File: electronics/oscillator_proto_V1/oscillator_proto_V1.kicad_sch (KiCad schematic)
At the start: 48 parts, among them J1 module_2x15_left_input, J2 module_2x15_right_input, J3 Coax, Q1 BC337, U1 TL081, U2 LME49720, U3 TL082, U4 TL431

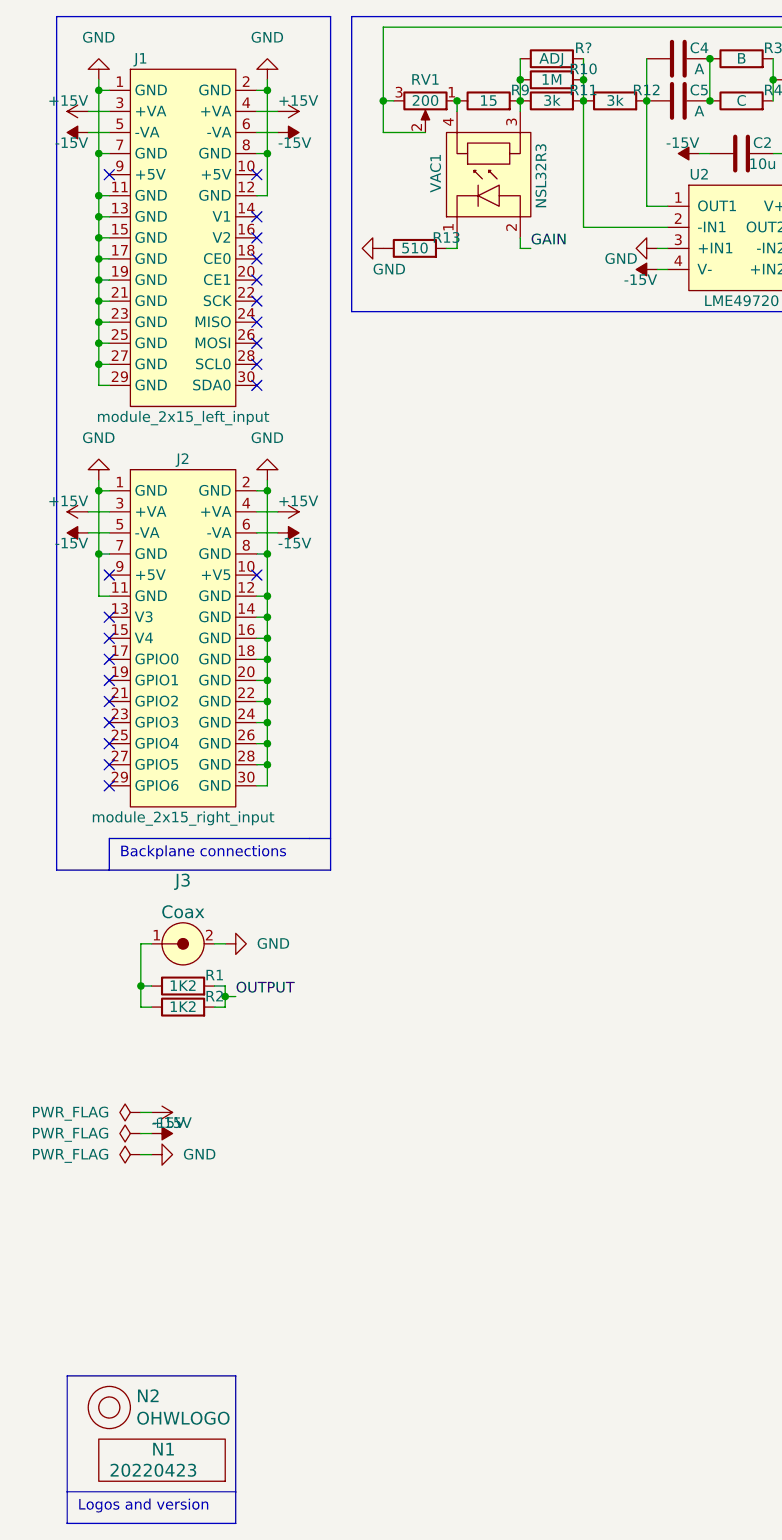
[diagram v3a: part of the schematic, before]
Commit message: added additional adjust resistor and updated values
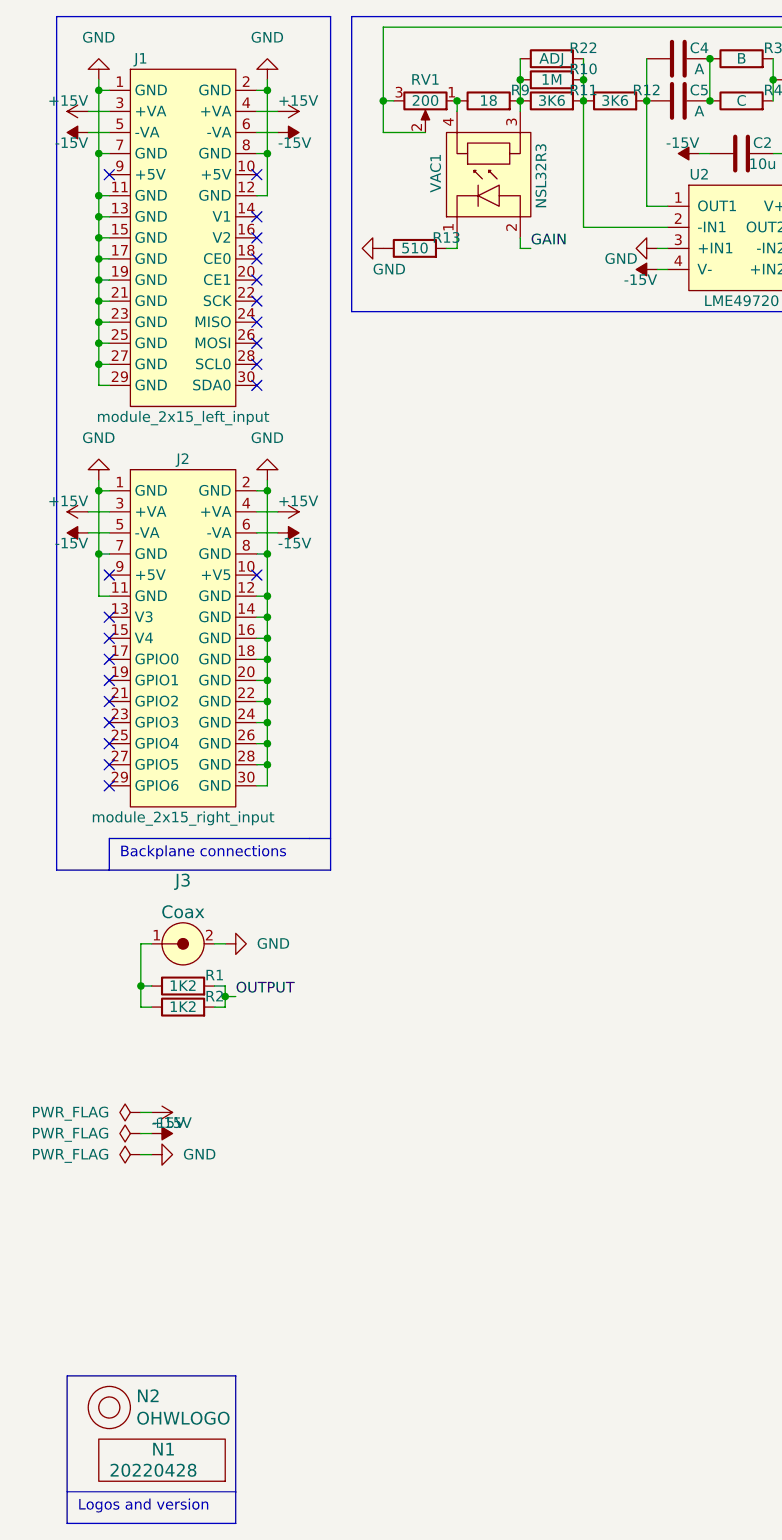
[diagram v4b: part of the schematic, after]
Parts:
- N1: value 20220423 -> 20220428
- R11, R12: value 3k -> 3K6
- R9: value 15 -> 18
- gave numbers to parts that had none: 1
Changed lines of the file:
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@@
       (effects (font (size 1.524 1.524)) (justify left))
     )
-    (property "Value" "20220423" (id 1) (at 20.32 189.23 0)
+    (property "Value" "20220428" (id 1) (at 20.32 189.23 0)
       (effects (font (size 1.524 1.524)) (justify left))
     )
@@
   (symbol (lib_id "Device:R") (at 73.66 19.05 90) (unit 1)
     (in_bom yes) (on_board yes)
-    (property "Reference" "R?" (id 0) (at 77.47 17.78 90))
+    (property "Reference" "R22" (id 0) (at 77.47 17.78 90))
     (property "Value" "ADJ" (id 1) (at 73.66 19.05 90))
     (property "Footprint" "SquantorRcl:R_0805+0603" (id 2) (at 73.66 20.828 90)
@@
     (in_bom yes) (on_board yes)
     (property "Reference" "R9" (id 0) (at 69.85 22.86 90))
-    (property "Value" "15" (id 1) (at 66.04 24.13 90))
+    (property "Value" "18" (id 1) (at 66.04 24.13 90))
     (property "Footprint" "SquantorRcl:R_0805+0603" (id 2) (at 66.04 25.908 90)
       (effects (font (size 1.27 1.27)) hide)
@@
     (in_bom yes) (on_board yes)
     (property "Reference" "R11" (id 0) (at 77.47 22.86 90))
-    (property "Value" "3k" (id 1) (at 73.66 24.13 90))
+    (property "Value" "3K6" (id 1) (at 73.66 24.13 90))
     (property "Footprint" "SquantorRcl:R_0805+0603" (id 2) (at 73.66 25.908 90)
       (effects (font (size 1.27 1.27)) hide)
@@
     (in_bom yes) (on_board yes)
     (property "Reference" "R12" (id 0) (at 85.09 22.86 90))
-    (property "Value" "3k" (id 1) (at 81.28 24.13 90))
+    (property "Value" "3K6" (id 1) (at 81.28 24.13 90))
     (property "Footprint" "SquantorRcl:R_0805+0603" (id 2) (at 81.28 25.908 90)
       (effects (font (size 1.27 1.27)) hide)
@@
     )
     (path "/00000000-0000-0000-0000-00005ee12bf3"
-      (reference "N1") (unit 1) (value "20220423") (footprint "SquantorLabels:Label_Generic")
+      (reference "N1") (unit 1) (value "20220428") (footprint "SquantorLabels:Label_Generic")
     )
     (path "/00000000-0000-0000-0000-00005ee13678"
@@
     )
     (path "/369ee294-bf66-474e-b6e0-37a03dbc4bc4"
-      (reference "R9") (unit 1) (value "15") (footprint "SquantorRcl:R_0805+0603")
+      (reference "R9") (unit 1) (value "18") (footprint "SquantorRcl:R_0805+0603")
     )
     (path "/01f8a0e7-26a2-4326-b183-3820289b3c31"
@@
     )
     (path "/41b19e5e-9b4d-4860-bc3b-2d98ed830408"
-      (reference "R11") (unit 1) (value "3k") (footprint "SquantorRcl:R_0805+0603")
+      (reference "R11") (unit 1) (value "3K6") (footprint "SquantorRcl:R_0805+0603")
     )
     (path "/fec7fcce-e8cc-4643-8ba6-1f09123fcd4f"
-      (reference "R12") (unit 1) (value "3k") (footprint "SquantorRcl:R_0805+0603")
+      (reference "R12") (unit 1) (value "3K6") (footprint "SquantorRcl:R_0805+0603")
     )
     (path "/c13e89fa-88d8-499c-b86a-4cbefd7d2011"
@@
     )
     (path "/21f01333-f32c-4c7a-b25c-e4d5d4e4359a"
-      (reference "R?") (unit 1) (value "ADJ") (footprint "SquantorRcl:R_0805+0603")
+      (reference "R22") (unit 1) (value "ADJ") (footprint "SquantorRcl:R_0805+0603")
     )
     (path "/afdcc91f-3c54-4dc6-8d8a-38d6d5d4d261"
